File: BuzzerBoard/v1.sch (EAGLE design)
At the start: 7 parts, among them U1 LM386MX-1/NOPB

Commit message: Initial schematic capture.
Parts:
- added J1: p0, SparkFun-Connectors:CONN_03SMD_RA_MALE
- added U$1: SMS-1308MS-2-R, BuzzerLib:SMS-1308MS-2-R
- R2: value 0R -> 10R
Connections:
- new net +: C4.22, U$1.+
- new net 3.3V: J1.2, U1.VS
- new net BYPASS: C3.1, U1.BYPASS
- new net GAIN: C1.2, U1.GAIN
- new net GND: C3.2, J1.1, R1.1, R2.1, U$1.-, U1.GND, U1.IN-
- new net IN+: R1.2, U1.IN+
- new net N$1: C2.2, R2.2
- new net N$2: C1.1, U1.GAIN_2
- new net N$3: C2.1, C4.11, U1.VOUT
- new net P0: J1.3, R1.3
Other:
- moved on the sheet: C1, C2, C3, C4, R1, R2, U1
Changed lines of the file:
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@@
 <part name="C2" library="SparkFun-Capacitors" library_urn="urn:adsk.eagle:library:510" deviceset="47NF" device="-0603-25V-5%" package3d_urn="urn:adsk.eagle:package:37414/1" value="47nF"/>
 <part name="C3" library="SparkFun-Capacitors" library_urn="urn:adsk.eagle:library:510" deviceset="0.1UF" device="-0603-25V-(+80/-20%)" package3d_urn="urn:adsk.eagle:package:37414/1" value="0.1uF"/>
-<part name="R2" library="Seeed-Resistor" library_urn="urn:adsk.eagle:library:474" deviceset="SMD-RES-0R-5%-1/10W(0603)" device="" package3d_urn="urn:adsk.eagle:package:32791/1" value="0R"/>
+<part name="R2" library="Seeed-Resistor" library_urn="urn:adsk.eagle:library:474" deviceset="SMD-RES-0R-5%-1/10W(0603)" device="" package3d_urn="urn:adsk.eagle:package:32791/1" value="10R"/>
 <part name="C4" library="BuzzerLib" deviceset="6SVPE220MW" device=""/>
+<part name="U$1" library="BuzzerLib" deviceset="SMS-1308MS-2-R" device=""/>
+<part name="J1" library="SparkFun-Connectors" library_urn="urn:adsk.eagle:library:513" deviceset="CONN_03" device="SMD_RA_MALE" package3d_urn="urn:adsk.eagle:package:38078/1" value="p0"/>
+<part name="GND" library="SparkFun-PowerSymbols" library_urn="urn:adsk.eagle:library:530" deviceset="GND2" device="" value="GND"/>
 </parts>
 <sheets>
@@
 </plain>
 <instances>
-<instance part="U1" gate="A" x="5.08" y="20.32"/>
-<instance part="R1" gate="A" x="15.24" y="55.88"/>
-<instance part="C1" gate="G$1" x="81.28" y="0"/>
-<instance part="C2" gate="G$1" x="83.82" y="35.56"/>
-<instance part="C3" gate="G$1" x="96.52" y="15.24"/>
-<instance part="R2" gate="G$1" x="93.98" y="-2.54" rot="R90"/>
-<instance part="C4" gate="A" x="78.74" y="60.96"/>
+<instance part="U1" gate="A" x="50.8" y="20.32"/>
+<instance part="R1" gate="A" x="43.18" y="22.86" smashed="yes" rot="R180">
+<attribute name="VALUE" x="26.3144" y="30.8864" size="2.0828" layer="96" ratio="6" rot="SR180"/>
+<attribute name="NAME" x="25.6794" y="34.6964" size="2.0828" layer="95" ratio="6" rot="SR180"/>
+</instance>
+<instance part="C1" gate="G$1" x="83.82" y="40.64" rot="R90"/>
+<instance part="C2" gate="G$1" x="132.08" y="2.54"/>
+<instance part="C3" gate="G$1" x="111.76" y="-5.08"/>
+<instance part="R2" gate="G$1" x="132.08" y="-5.08" rot="R90"/>
+<instance part="C4" gate="A" x="137.16" y="12.7" smashed="yes">
+<attribute name="VALUE" x="134.7978" y="15.7988" size="1.778" layer="96" ratio="10" rot="SR0"/>
+<attribute name="NAME" x="138.1506" y="9.7028" size="1.778" layer="95" ratio="10" rot="SR0"/>
+</instance>
+<instance part="U$1" gate="G$1" x="154.94" y="8.89"/>
+<instance part="J1" gate="J$1" x="-15.24" y="15.24"/>
+<instance part="GND" gate="G$1" x="83.82" y="-15.24"/>
 </instances>
 <busses>
 </busses>
 <nets>
+<net name="IN+" class="0">
+<segment>
+<pinref part="R1" gate="A" pin="2"/>
+<pinref part="U1" gate="A" pin="IN+"/>
+<wire x1="33.02" y1="15.24" x2="53.34" y2="15.24" width="0.1524" layer="91"/>
+</segment>
+</net>
+<net name="P0" class="0">
+<segment>
+<pinref part="J1" gate="J$1" pin="3"/>
+<wire x1="-7.62" y1="17.78" x2="-5.08" y2="17.78" width="0.1524" layer="91"/>
+<wire x1="-5.08" y1="17.78" x2="-5.08" y2="22.86" width="0.1524" layer="91"/>
+<pinref part="R1" gate="A" pin="3"/>
+<wire x1="-5.08" y1="22.86" x2="0" y2="22.86" width="0.1524" layer="91"/>
+<label x="-8.128" y="18.288" size="1.778" layer="95"/>
+</segment>
+</net>
+<net name="3.3V" class="0">
+<segment>
+<pinref part="J1" gate="J$1" pin="2"/>
+<wire x1="-7.62" y1="15.24" x2="2.54" y2="15.24" width="0.1524" layer="91"/>
+<label x="-2.032" y="15.748" size="1.778" layer="95"/>
+</segment>
+<segment>
+<pinref part="U1" gate="A" pin="VS"/>
+<wire x1="114.3" y1="15.24" x2="124.46" y2="15.24" width="0.1524" layer="91"/>
+<label x="119.888" y="15.494" size="1.778" layer="95"/>
+</segment>
+</net>
+<net name="GND" class="0">
+<segment>
+<pinref part="U1" gate="A" pin="GND"/>
+<wire x1="-7.62" y1="12.7" x2="38.1" y2="12.7" width="0.1524" layer="91"/>
+<pinref part="J1" gate="J$1" pin="1"/>
+<wire x1="38.1" y1="12.7" x2="40.64" y2="12.7" width="0.1524" layer="91"/>
+<wire x1="40.64" y1="12.7" x2="43.18" y2="12.7" width="0.1524" layer="91"/>
+<wire x1="43.18" y1="12.7" x2="53.34" y2="12.7" width="0.1524" layer="91"/>
+<pinref part="R1" gate="A" pin="1"/>
+<wire x1="40.64" y1="22.86" x2="40.64" y2="12.7" width="0.1524" layer="91"/>
+<junction x="40.64" y="12.7"/>
+<pinref part="U1" gate="A" pin="IN-"/>
+<wire x1="53.34" y1="17.78" x2="43.18" y2="17.78" width="0.1524" layer="91"/>
+<wire x1="43.18" y1="17.78" x2="43.18" y2="12.7" width="0.1524" layer="91"/>
+<junction x="43.18" y="12.7"/>
+<pinref part="GND" gate="G$1" pin="3.3V"/>
+<wire x1="83.82" y1="-12.7" x2="38.1" y2="-12.7" width="0.1524" layer="91"/>
+<wire x1="38.1" y1="-12.7" x2="38.1" y2="12.7" width="0.1524" layer="91"/>
+<junction x="38.1" y="12.7"/>
+<label x="-8.636" y="12.954" size="1.778" layer="95"/>
+<wire x1="83.82" y1="-12.7" x2="111.76" y2="-12.7" width="0.1524" layer="91"/>
+<wire x1="111.76" y1="-12.7" x2="132.08" y2="-12.7" width="0.1524" layer="91"/>
+<wire x1="132.08" y1="-12.7" x2="147.32" y2="-12.7" width="0.1524" layer="91"/>
+<wire x1="147.32" y1="-12.7" x2="147.32" y2="10.16" width="0.1524" layer="91"/>
+<junction x="83.82" y="-12.7"/>
+<pinref part="U$1" gate="G$1" pin="-"/>
+<wire x1="147.32" y1="10.16" x2="152.4" y2="10.16" width="0.1524" layer="91"/>
+<pinref part="C3" gate="G$1" pin="2"/>
+<wire x1="111.76" y1="-7.62" x2="111.76" y2="-12.7" width="0.1524" layer="91"/>
+<junction x="111.76" y="-12.7"/>
+<pinref part="R2" gate="G$1" pin="1"/>
+<wire x1="132.08" y1="-8.89" x2="132.08" y2="-12.7" width="0.1524" layer="91"/>
+<junction x="132.08" y="-12.7"/>
+</segment>
+</net>
+<net name="+" class="0">
+<segment>
+<pinref part="C4" gate="A" pin="22"/>
+<pinref part="U$1" gate="G$1" pin="+"/>
+<wire x1="144.78" y1="12.7" x2="152.4" y2="12.7" width="0.1524" layer="91"/>
+</segment>
+</net>
+<net name="GAIN" class="0">
+<segment>
+<pinref part="U1" gate="A" pin="GAIN"/>
+<wire x1="132.08" y1="20.32" x2="114.3" y2="20.32" width="0.1524" layer="91"/>
+<pinref part="C1" gate="G$1" pin="2"/>
+<wire x1="86.36" y1="40.64" x2="132.08" y2="40.64" width="0.1524" layer="91"/>
+<wire x1="132.08" y1="40.64" x2="132.08" y2="20.32" width="0.1524" layer="91"/>
+</segment>
+</net>
+<net name="BYPASS" class="0">
+<segment>
+<pinref part="C3" gate="G$1" pin="1"/>
+<wire x1="111.76" y1="0" x2="111.76" y2="5.08" width="0.1524" layer="91"/>
+<label x="102.616" y="3.302" size="1.778" layer="95"/>
+</segment>
+<segment>
+<pinref part="U1" gate="A" pin="BYPASS"/>
+<wire x1="114.3" y1="17.78" x2="124.46" y2="17.78" width="0.1524" layer="91"/>
+<label x="116.078" y="18.034" size="1.778" layer="95"/>
+</segment>
+</net>
+<net name="N$1" class="0">
+<segment>
+<pinref part="R2" gate="G$1" pin="2"/>
+<pinref part="C2" gate="G$1" pin="2"/>
+<wire x1="132.08" y1="-1.27" x2="132.08" y2="0" width="0.1524" layer="91"/>
+</segment>
+</net>
+<net name="N$2" class="0">
+<segment>
+<pinref part="U1" gate="A" pin="GAIN_2"/>
+<wire x1="53.34" y1="20.32" x2="48.26" y2="20.32" width="0.1524" layer="91"/>
+<wire x1="48.26" y1="20.32" x2="48.26" y2="40.64" width="0.1524" layer="91"/>
+<pinref part="C1" gate="G$1" pin="1"/>
+<wire x1="48.26" y1="40.64" x2="78.74" y2="40.64" width="0.1524" layer="91"/>
+</segment>
+</net>
+<net name="N$3" class="0">
+<segment>
+<pinref part="C4" gate="A" pin="11"/>
+<wire x1="137.16" y1="12.7" x2="132.08" y2="12.7" width="0.1524" layer="91"/>
+<pinref part="C2" gate="G$1" pin="1"/>
+<wire x1="132.08" y1="7.62" x2="132.08" y2="12.7" width="0.1524" layer="91"/>
+<pinref part="U1" gate="A" pin="VOUT"/>
+<wire x1="114.3" y1="12.7" x2="132.08" y2="12.7" width="0.1524" layer="91"/>
+<junction x="132.08" y="12.7"/>
+</segment>
+</net>
 </nets>
 </sheet>
 </sheets>
+<errors>
+</errors>
 </schematic>
 </drawing>

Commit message: V1 to OSH park.
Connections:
- net N$3 renamed VOUT
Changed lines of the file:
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@@
 </segment>
 </net>
-<net name="N$3" class="0">
+<net name="VOUT" class="0">
 <segment>
 <pinref part="C4" gate="A" pin="11"/>

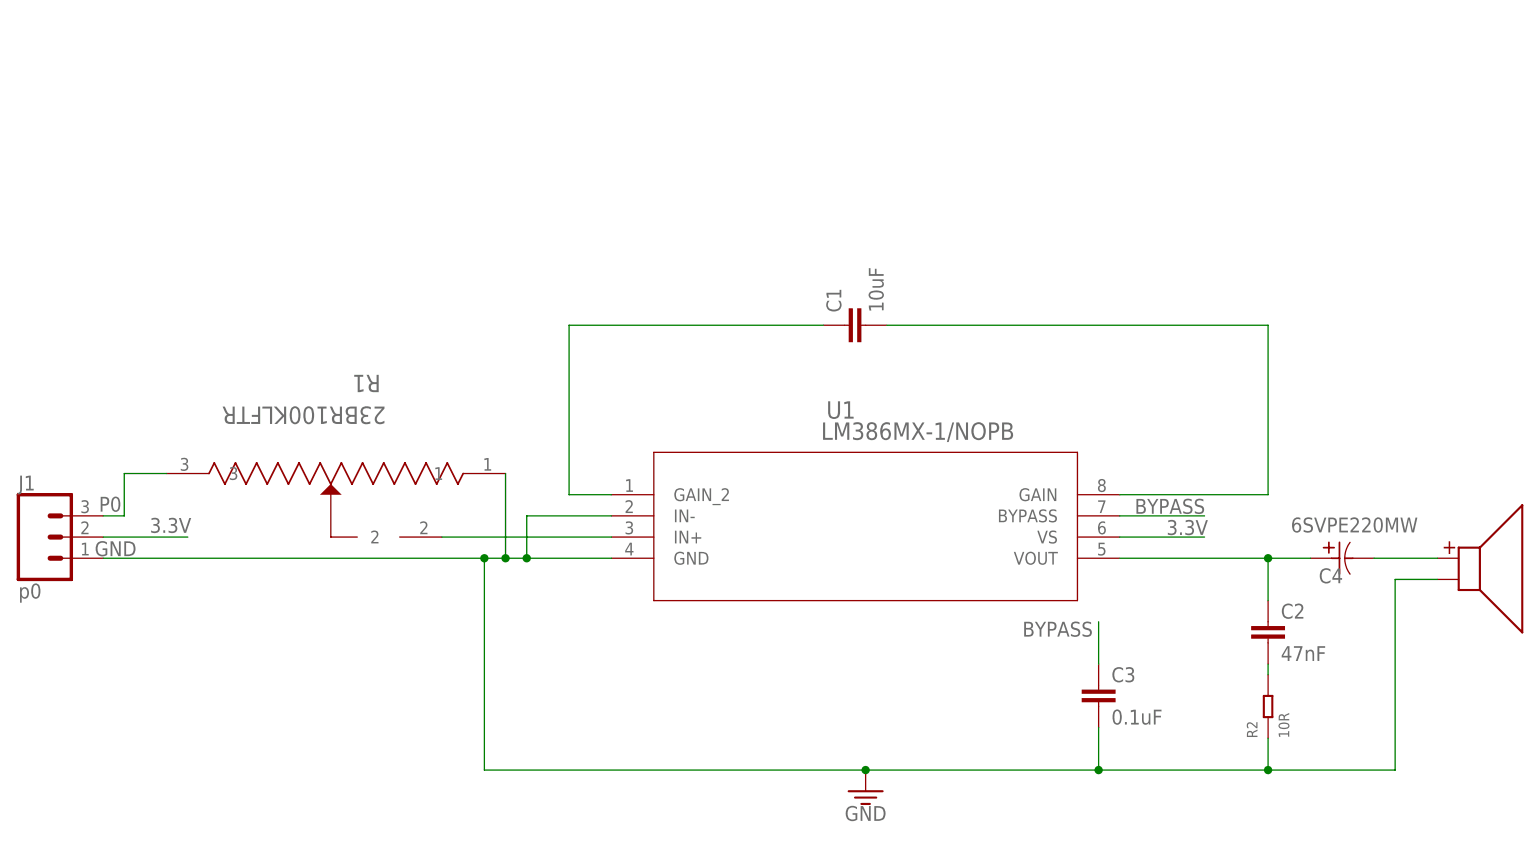
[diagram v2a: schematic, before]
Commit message: Adding pdf of schematic and board.
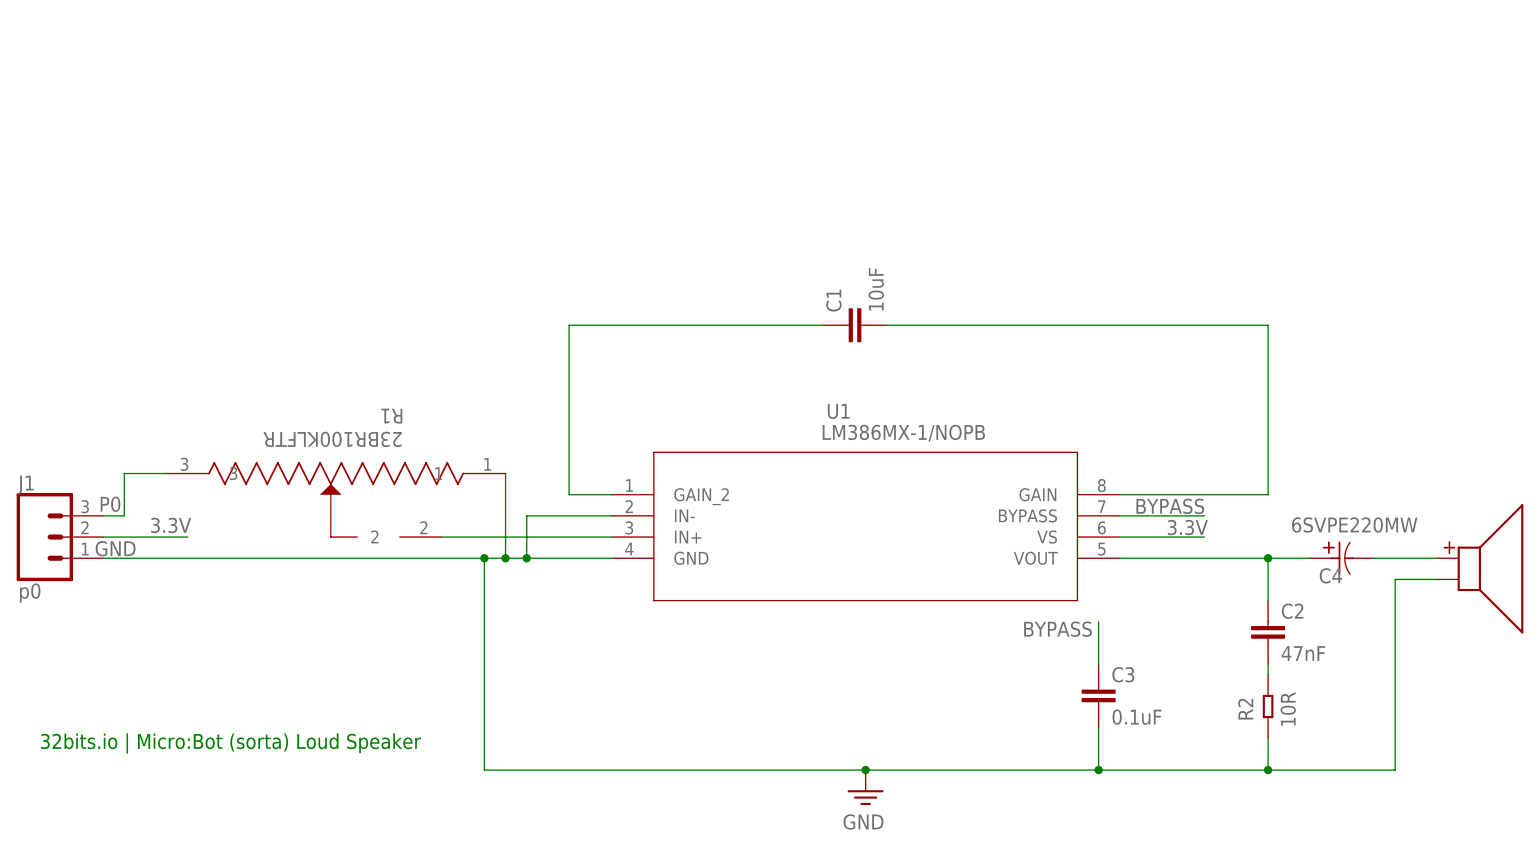
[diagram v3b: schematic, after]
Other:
- note added: "32bits.io | Micro:Bot (sorta) Loud Speaker"
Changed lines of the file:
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@@
 <sheet>
 <plain>
+<text x="-15.24" y="-10.16" size="1.778" layer="91">32bits.io | Micro:Bot (sorta) Loud Speaker</text>
 </plain>
 <instances>
-<instance part="U1" gate="A" x="50.8" y="20.32"/>
+<instance part="U1" gate="A" x="50.8" y="20.32" smashed="yes">
+<attribute name="NAME" x="79.0956" y="29.4386" size="1.778" layer="95" ratio="10" rot="SR0"/>
+<attribute name="VALUE" x="78.4606" y="26.8986" size="1.778" layer="96" ratio="10" rot="SR0"/>
+</instance>
 <instance part="R1" gate="A" x="43.18" y="22.86" smashed="yes" rot="R180">
-<attribute name="VALUE" x="26.3144" y="30.8864" size="2.0828" layer="96" ratio="6" rot="SR180"/>
-<attribute name="NAME" x="25.6794" y="34.6964" size="2.0828" layer="95" ratio="6" rot="SR180"/>
+<attribute name="VALUE" x="28.3464" y="27.8384" size="1.778" layer="96" ratio="10" rot="SR180"/>
+<attribute name="NAME" x="28.4734" y="30.6324" size="1.778" layer="95" ratio="10" rot="SR180"/>
 </instance>
-<instance part="C1" gate="G$1" x="83.82" y="40.64" rot="R90"/>
+<instance part="C1" gate="G$1" x="83.82" y="40.64" smashed="yes" rot="R90">
+<attribute name="NAME" x="80.899" y="42.164" size="1.778" layer="95" font="vector" ratio="10" rot="R90"/>
+<attribute name="VALUE" x="85.979" y="42.164" size="1.778" layer="96" font="vector" ratio="10" rot="R90"/>
+</instance>
 <instance part="C2" gate="G$1" x="132.08" y="2.54"/>
 <instance part="C3" gate="G$1" x="111.76" y="-5.08"/>
-<instance part="R2" gate="G$1" x="132.08" y="-5.08" rot="R90"/>
+<instance part="R2" gate="G$1" x="132.08" y="-5.08" smashed="yes" rot="R90">
+<attribute name="NAME" x="130.302" y="-6.858" size="1.778" layer="95" ratio="10" rot="R90"/>
+<attribute name="VALUE" x="135.382" y="-7.62" size="1.778" layer="96" ratio="10" rot="R90"/>
+</instance>
 <instance part="C4" gate="A" x="137.16" y="12.7" smashed="yes">
 <attribute name="VALUE" x="134.7978" y="15.7988" size="1.778" layer="96" ratio="10" rot="SR0"/>
@@
 <instance part="U$1" gate="G$1" x="154.94" y="8.89"/>
 <instance part="J1" gate="J$1" x="-15.24" y="15.24"/>
-<instance part="GND" gate="G$1" x="83.82" y="-15.24"/>
+<instance part="GND" gate="G$1" x="83.82" y="-15.24" smashed="yes">
+<attribute name="VALUE" x="83.566" y="-18.034" size="1.778" layer="96" font="vector" ratio="10" align="top-center"/>
+</instance>
 </instances>
 <busses>
@@
 <pinref part="J1" gate="J$1" pin="2"/>
 <wire x1="-7.62" y1="15.24" x2="2.54" y2="15.24" width="0.1524" layer="91"/>
-<label x="-2.032" y="15.748" size="1.778" layer="95"/>
+<label x="-2.032" y="15.748" size="1.778" layer="95" ratio="10"/>
 </segment>
 <segment>
 <pinref part="U1" gate="A" pin="VS"/>
 <wire x1="114.3" y1="15.24" x2="124.46" y2="15.24" width="0.1524" layer="91"/>
-<label x="119.888" y="15.494" size="1.778" layer="95"/>
+<label x="119.888" y="15.494" size="1.778" layer="95" ratio="10"/>
 </segment>
 </net>
